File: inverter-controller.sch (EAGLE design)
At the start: 187 parts, among them IC1 STM32F334C8T6, IC2 SY7152ABC, IC3 LMV358MMX, IC4 LMV358MMX, IC5 SY7152ABC, J1 621006245821, J2 61300211121, K1 FINDER_34.51.7.024.0010FINDER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, K2 FINDER_34.51.7.024.0010FINDER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, K3 FINDER_34.51.7.024.0010FINDER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, U1 DIODES_AP3015KTR-G1DIODES_AP3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, X1 0289-9066**15EDGVC-3.81-02P-14, X2 0289-9066**15EDGVC-3.81-02P-14, X3 0289-9066**15EDGVC-3.81-02P-14, X4 0289-9066**15EDGVC-3.81-02P-14, X5 1365-10, X6 1365-16, X7 1365-10, X8 1365-10, Y1 NX2016SA-32M

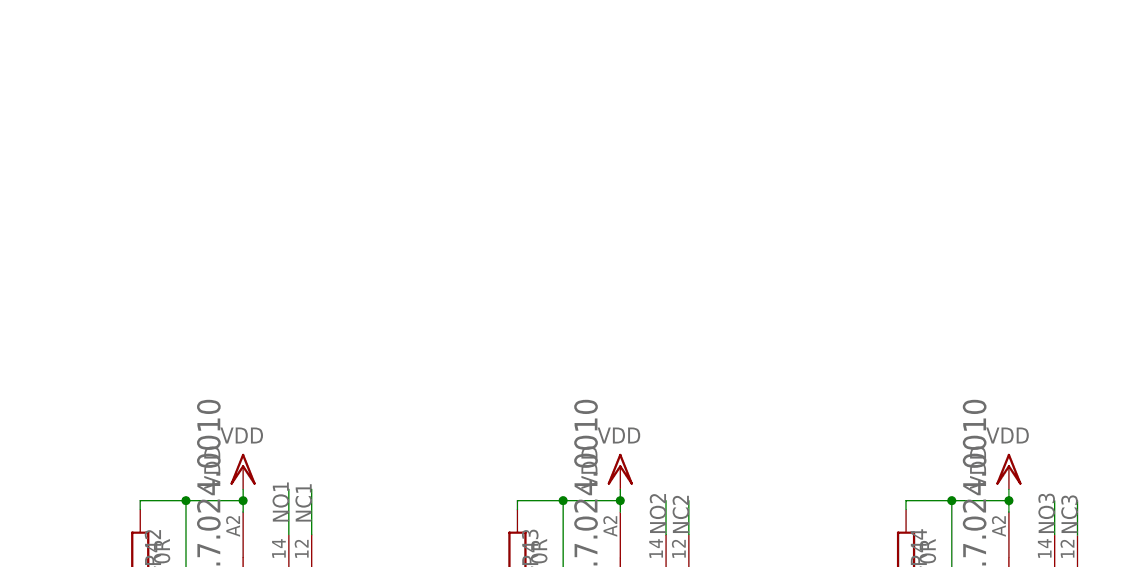
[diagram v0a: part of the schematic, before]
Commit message: Relay soketleri eklendi.
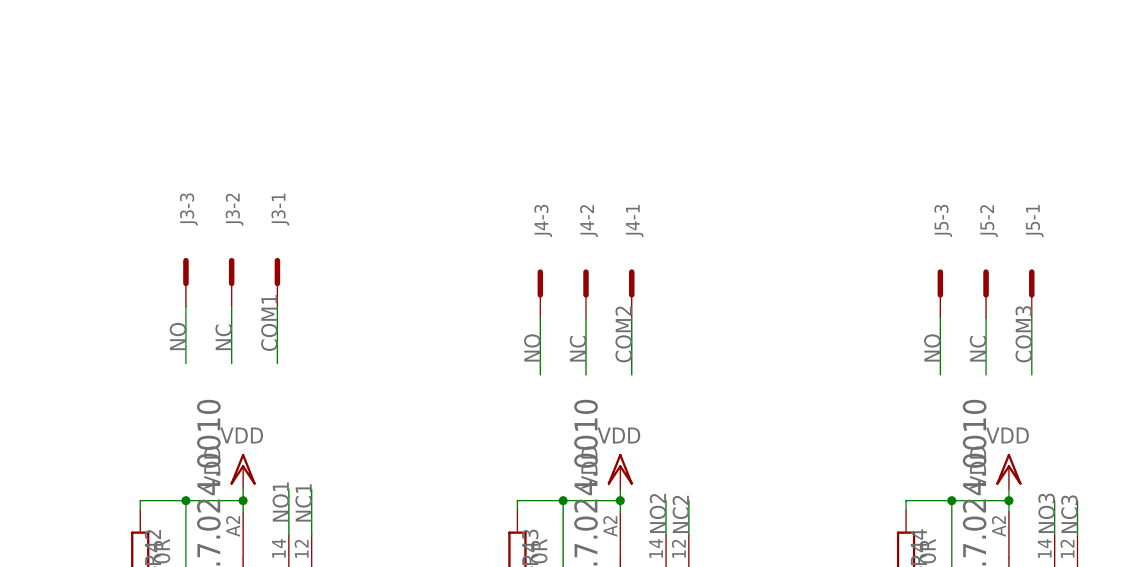
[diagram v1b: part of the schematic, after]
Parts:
- added J3, J4, J5: MCV3, con-phoenix-381:MCV3
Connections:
- new net NC: J3-2.SK, J4-2.SK, J5-2.SK
- new net NO: J3-3.SK, J4-3.SK, J5-3.SK
- net COM1: now also J3-1.SK
- net COM2: now also J4-1.SK
- net COM3: now also J5-1.SK
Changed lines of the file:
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@@
 <part name="GND48" library="supply1" library_urn="urn:adsk.eagle:library:371" deviceset="GND" device=""/>
 <part name="GND49" library="supply1" library_urn="urn:adsk.eagle:library:371" deviceset="GND" device=""/>
+<part name="J3" library="con-phoenix-381" library_urn="urn:adsk.eagle:library:27486877" deviceset="MCV3" device="" package3d_urn="urn:adsk.eagle:package:27487037/1"/>
+<part name="J4" library="con-phoenix-381" library_urn="urn:adsk.eagle:library:27486877" deviceset="MCV3" device="" package3d_urn="urn:adsk.eagle:package:27487037/1"/>
+<part name="J5" library="con-phoenix-381" library_urn="urn:adsk.eagle:library:27486877" deviceset="MCV3" device="" package3d_urn="urn:adsk.eagle:package:27487037/1"/>
 </parts>
 <sheets>
@@
 <attribute name="VALUE" x="179.07" y="145.288" size="1.778" layer="96" rot="R270"/>
 </instance>
+<instance part="J3" gate="-1" x="387.35" y="261.62" smashed="yes" rot="R270">
+<attribute name="NAME" x="386.715" y="271.78" size="1.524" layer="95" rot="R270"/>
+</instance>
+<instance part="J3" gate="-2" x="382.27" y="261.62" smashed="yes" rot="R270">
+<attribute name="NAME" x="381.635" y="271.78" size="1.524" layer="95" rot="R270"/>
+</instance>
+<instance part="J3" gate="-3" x="377.19" y="261.62" smashed="yes" rot="R270">
+<attribute name="NAME" x="376.555" y="271.78" size="1.524" layer="95" rot="R270"/>
+</instance>
+<instance part="J4" gate="-1" x="426.72" y="260.35" smashed="yes" rot="R270">
+<attribute name="NAME" x="426.085" y="270.51" size="1.524" layer="95" rot="R270"/>
+</instance>
+<instance part="J4" gate="-2" x="421.64" y="260.35" smashed="yes" rot="R270">
+<attribute name="NAME" x="421.005" y="270.51" size="1.524" layer="95" rot="R270"/>
+</instance>
+<instance part="J4" gate="-3" x="416.56" y="260.35" smashed="yes" rot="R270">
+<attribute name="NAME" x="415.925" y="270.51" size="1.524" layer="95" rot="R270"/>
+</instance>
+<instance part="J5" gate="-1" x="471.17" y="260.35" smashed="yes" rot="R270">
+<attribute name="NAME" x="470.535" y="270.51" size="1.524" layer="95" rot="R270"/>
+</instance>
+<instance part="J5" gate="-2" x="466.09" y="260.35" smashed="yes" rot="R270">
+<attribute name="NAME" x="465.455" y="270.51" size="1.524" layer="95" rot="R270"/>
+</instance>
+<instance part="J5" gate="-3" x="461.01" y="260.35" smashed="yes" rot="R270">
+<attribute name="NAME" x="460.375" y="270.51" size="1.524" layer="95" rot="R270"/>
+</instance>
 </instances>
 <busses>
@@
 <label x="388.62" y="212.09" size="1.778" layer="95" rot="R90"/>
 </segment>
+<segment>
+<pinref part="J3" gate="-1" pin="SK"/>
+<wire x1="387.35" y1="259.08" x2="387.35" y2="252.73" width="0.1524" layer="91"/>
+<label x="387.35" y="254" size="1.778" layer="95" rot="R90"/>
+</segment>
 </net>
 <net name="NO2" class="0">
@@
 <label x="430.53" y="212.09" size="1.778" layer="95" rot="R90"/>
 </segment>
+<segment>
+<pinref part="J4" gate="-1" pin="SK"/>
+<wire x1="426.72" y1="257.81" x2="426.72" y2="251.46" width="0.1524" layer="91"/>
+<label x="426.72" y="252.73" size="1.778" layer="95" rot="R90"/>
+</segment>
 </net>
 <net name="COM3" class="0">
@@
 <label x="473.71" y="212.09" size="1.778" layer="95" rot="R90"/>
 </segment>
+<segment>
+<pinref part="J5" gate="-1" pin="SK"/>
+<wire x1="471.17" y1="257.81" x2="471.17" y2="251.46" width="0.1524" layer="91"/>
+<label x="471.17" y="252.73" size="1.778" layer="95" rot="R90"/>
+</segment>
 </net>
 <net name="NO3" class="0">
@@
 </segment>
 </net>
+<net name="NC" class="0">
+<segment>
+<pinref part="J3" gate="-2" pin="SK"/>
+<wire x1="382.27" y1="259.08" x2="382.27" y2="252.73" width="0.1524" layer="91"/>
+<label x="382.27" y="254" size="1.778" layer="95" rot="R90"/>
+</segment>
+<segment>
+<pinref part="J4" gate="-2" pin="SK"/>
+<wire x1="421.64" y1="257.81" x2="421.64" y2="251.46" width="0.1524" layer="91"/>
+<label x="421.64" y="252.73" size="1.778" layer="95" rot="R90"/>
+</segment>
+<segment>
+<pinref part="J5" gate="-2" pin="SK"/>
+<wire x1="466.09" y1="257.81" x2="466.09" y2="251.46" width="0.1524" layer="91"/>
+<label x="466.09" y="252.73" size="1.778" layer="95" rot="R90"/>
+</segment>
+</net>
+<net name="NO" class="0">
+<segment>
+<pinref part="J3" gate="-3" pin="SK"/>
+<wire x1="377.19" y1="259.08" x2="377.19" y2="252.73" width="0.1524" layer="91"/>
+<label x="377.19" y="254" size="1.778" layer="95" rot="R90"/>
+</segment>
+<segment>
+<pinref part="J4" gate="-3" pin="SK"/>
+<wire x1="416.56" y1="257.81" x2="416.56" y2="251.46" width="0.1524" layer="91"/>
+<label x="416.56" y="252.73" size="1.778" layer="95" rot="R90"/>
+</segment>
+<segment>
+<pinref part="J5" gate="-3" pin="SK"/>
+<wire x1="461.01" y1="257.81" x2="461.01" y2="251.46" width="0.1524" layer="91"/>
+<label x="461.01" y="252.73" size="1.778" layer="95" rot="R90"/>
+</segment>
+</net>

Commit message: Mekanik kistaslar belirlendi.
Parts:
- removed D7: (no value), diode:DIODE-SOD80C
- removed J5: MCV3, con-phoenix-381:MCV3
- removed K3: FINDER_34.51.7.024.0010FINDER_34.51.7.024.0010_0_0, Finder - 34.51.7.024.0010:FINDER_34.51.7.024.0010FINDER_34.51.7.024.0010_0_0
- removed LED3: (no value), adafruit:LEDCHIPLED_0805
- removed Q3: (no value), adafruit:MOSFET-NREFLOW
- removed R40: (no value), rcl:R-EU_R0603
- removed R41: 22R, rcl:R-EU_R0603
- removed R44: 470R, rcl:R-EU_R0603
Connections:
- removed net COM3: J5-1.SK, K3.11
- removed net N$28: Q3.G, R40.2, R41.1
- removed net N$31: D7.A, K3.A1, LED3.C, Q3.D
- removed net N$33: LED3.A, R44.1
- removed net NC3: K3.12
- removed net NO3: K3.14
- net GND: no longer Q3.S, R40.1
- net NC: no longer J5-2.SK
- net NO: no longer J5-3.SK
- net RELAY3: no longer R41.2
- net VDD: no longer D7.C, K3.A2, R44.2

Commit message: Mini kart tasarimi icin sadelestirildi.
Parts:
- removed C20, C60, C63: 100n, rcl:C-EUC0603
- removed C59: 1019-3366**CAP 0603 CER 10uF 16V %20 X5R, rcl:C-EUC0603
- removed C61: 10n, rcl:C-EUC0603
- removed C62: 1n, rcl:C-EUC0603
- removed C64: 1u, rcl:C-EUC1206
- removed D5, D6: (no value), diode:DIODE-SOD80C
- removed D9: 1119-3055, Diode:DIODEDO-214AC(SMA)
- removed J3, J4: MCV3, con-phoenix-381:MCV3
- removed K1, K2: FINDER_34.51.7.024.0010FINDER_34.51.7.024.0010_0_0, Finder - 34.51.7.024.0010:FINDER_34.51.7.024.0010FINDER_34.51.7.024.0010_0_0
- removed L2: 1319-4102**INDUCTOR POWER 22UH 4X4X1.8MM SMD, wuerth-elektronik:WE-PD2_S
- removed LED1, LED11, LED2, LED4, LED5, LED6: (no value), adafruit:LEDCHIPLED_0805
- removed Q1, Q2: (no value), adafruit:MOSFET-NREFLOW
- removed R16, R37, R38: (no value), rcl:R-EU_R0603
- removed R36, R39: 22R, rcl:R-EU_R0603
- removed R42, R43: 470R, rcl:R-EU_R0603
- removed R45, R46, R47: 100R, rcl:R-EU_R0603
- removed R67: 2M, rcl:R-EU_R0603
- removed R68: 130K, rcl:R-EU_R0603
- removed R69: 1k, rcl:R-EU_R0603
- removed R73: NC, rcl:R-EU_R0603
- removed U1: DIODES_AP3015KTR-G1DIODES_AP3015KTR-G1_0_0, AP3015KTR-G1:DIODES_AP3015KTR-G1DIODES_AP3015KTR-G1_0_0
- removed X3: 0289-9066**15EDGVC-3.81-02P-14, con-phoenix-381_l:MCV2
- removed X5, X7, X8: 1365-10, con-leotronics:1365-10
- R56: value (none) -> 220R
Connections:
- removed net CAN_RX: IC1.PB8, X5-7.S, X5-8.S
- removed net CAN_TX: IC1.PB9, X5-5.S, X5-6.S
- removed net COM1: J3-1.SK, K1.11
- removed net COM2: J4-1.SK, K2.11
- removed net N$22: LED2.A, R43.1
- removed net N$24: Q1.G, R36.1, R37.2
- removed net N$25: Q2.G, R38.2, R39.1
- removed net N$26: LED5.A, R46.1
- removed net N$27: LED1.A, R42.1
- removed net N$29: D5.A, K1.A1, LED1.C, Q1.D
- removed net N$30: D6.A, K2.A1, LED2.C, Q2.D
- removed net N$32: LED6.A, R47.1
- removed net N$37: LED4.A, R45.1
- removed net N$44: D9.A, L2.1, U1.SW
- removed net N$45: R67.1, R68.2, U1.FB
- removed net N$49: LED11.A, R69.1
- removed net N$50: C59.1, C60.1, C61.1, L2.2, R73.2, U1.VIN
- removed net NC: J3-2.SK, J4-2.SK
- removed net NC1: K1.12
- removed net NC2: K2.12
- removed net NO: J3-3.SK, J4-3.SK
- removed net NO1: K1.14
- removed net NO2: K2.14
- removed net RELAY1: IC1.PB10, R36.2
- removed net RELAY2: IC1.PB11, R39.2
- removed net SPI1_CS: IC1.PA15, X8-10.S, X8-9.S
- removed net SPI1_MISO: IC1.PB4, X8-5.S, X8-6.S
- removed net SPI1_MOSI: IC1.PB5, X8-3.S, X8-4.S
- removed net USART1_RX: IC1.PB7, X7-7.S, X7-8.S
- removed net USART1_TX: IC1.PB6, X7-5.S, X7-6.S
- removed net VDD: C62.1, C63.1, C64.1, D5.C, D6.C, D9.C, K1.A2, K2.A2, R42.2, R43.2, R67.2, R69.2
- net +3V3: now also X6-1.S; no longer R73.1, X3.1.SK, X5-1.S, X5-2.S, X6-2.S, X7-1.S, X7-2.S, X8-1.S
- net DGND: now also X6-2.S; no longer X5-10.S, X5-3.S, X5-4.S, X5-9.S, X6-1.S, X7-3.S, X7-4.S, X8-2.S
- net DRV1_EN: now also X6-10.S; no longer X6-9.S
- net DRV2_EN: now also X6-4.S; no longer X6-3.S
- net G11_PWM: now also X6-14.S; no longer X6-13.S
- net G12_PWM: now also X6-12.S; no longer X6-11.S
- net G13_PWM: now also X6-8.S; no longer X6-7.S
- net G14_PWM: now also X6-6.S; no longer X6-5.S
- net GND: no longer C20.2, C59.2, C60.2, C61.2, C62.2, C63.2, C64.2, LED11.C, LED4.C, LED5.C, LED6.C, Q1.S, Q2.S, R37.1, R38.1, R68.1, R8.1, U1.GND
- net IA_SENS: now also X6-7.S; no longer X6-8.S
- net IB_SENS: now also X6-3.S; no longer X6-4.S
- net IIN_SENS: now also R8.1, X6-16.S; no longer R16.2, X6-15.S
- net I_IN: now also R8.2; no longer R16.1
- net N$13: no longer R45.2
- net N$14: no longer R46.2
- net N$20: no longer R47.2
- net NTC2: no longer C20.1, R8.2, X3.2.SK
- net RELAY_EN: no longer IC1.PA14, U1.!SHDN!
- net SPI1_SCK: no longer IC1.PB3, X8-7.S, X8-8.S
- net USART1_DIR: no longer X7-10.S, X7-9.S
- net VA_SENS: now also X6-9.S; no longer X6-10.S
- net VB_SENS: now also X6-5.S; no longer X6-6.S
- net VIN_2: now also R15.2; no longer R15.1
- net VIN_SENS: now also R15.1, X6-15.S; no longer R15.2, X6-16.S
- net VIN_SENS_DIFF: now also X6-13.S; no longer X6-14.S
- net VOUT_SENS_DIFF: now also X6-11.S; no longer X6-12.S
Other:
- note removed: "Haberlesme Kart Baglantilari"
- note removed: "Relay Coil Supply"
- note removed: "Relays"
- moved on the sheet: C33, C34, C35, C36, R15, R8, X6-1, X6-10, X6-11, X6-12, X6-13, X6-14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

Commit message: Direnc ve kondansator kutuphaneleri degistirildi(silk sorunu nedeniyle).
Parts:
- removed C58: 100n, rcl:C-EUC0603
- removed LED10, LED7, LED9: (no value), adafruit:LEDCHIPLED_0805
- removed R51, R52, R62, R63, R64: 33R, rcl:R-EU_R0603
- removed R53, R54, R65, R66: 1k, rcl:R-EU_R0603
- removed R55, R76: 470R, rcl:R-EU_R0603
- removed R56: 220R, rcl:R-EU_R0603
- removed R57: 1M, rcl:R-EU_R0603
- removed R58: 200k, rcl:R-EU_R0603
- removed R59: 10.5k, rcl:R-EU_R0603
- removed R60, R61: 0R, rcl:R-EU_R0603
- removed R71, R75: NC, rcl:R-EU_R0603
- added C20: 10nF, rcl:C-EUC0603E
- added LED1, LED2, LED3: (no value), adafruit:LEDCHIP-LED0805
- added R16: 220R, rcl:R-EU_R0603E
- added R36, R37: 470R, rcl:R-EU_R0603E
- added R38, R39, R47: 33R, rcl:R-EU_R0603E
- added R40, R44: 1K, rcl:R-EU_R0603E
- added R41: 1M, rcl:R-EU_R0603E
- added R42: 200K, rcl:R-EU_R0603E
- added R43: 10.5K, rcl:R-EU_R0603E
- added R45, R46: 0R, rcl:R-EU_R0603E
- C1, C2: value (none) -> 10pF; device rcl:C-EUC0603 -> rcl:C-EUC0603E
- C10, C13, C19, C37, C38, C47: value 100n -> 100nF; device rcl:C-EUC0603 -> rcl:C-EUC0603E
- C11: value 4.7u -> 4.7uF; device rcl:C-EUC0603 -> rcl:C-EUC0603E
- C12: value 1019-3366**CAP 0603 CER 10uF 16V %20 X5R -> 10uF; device rcl:C-EUC0603 -> rcl:C-EUC0603E
- C14, C3, C39, C48, C5, C52, C57: value 10n -> 10nF; device rcl:C-EUC0603 -> rcl:C-EUC0603E
- C15, C16, C54: value 10u -> 10uF; device rcl:C-EUC0805 -> rcl:C-EUC0603E
- C17, C22, C24, C26, C28, C30, C32, C34, C42, C45, C51: value 100n -> 10nF; device rcl:C-EUC0603 -> rcl:C-EUC0603E
- C18, C21, C23, C25, C27, C29, C31, C33, C35, C43, C46, C56: value 10n -> 100nF; device rcl:C-EUC0603 -> rcl:C-EUC0603E
- C36: value 100n -> 120pF; device rcl:C-EUC0603 -> rcl:C-EUC0603E
- C4: value 1u -> 1uF; device rcl:C-EUC0603 -> rcl:C-EUC0603E
- C40: value 120p -> 100nF; device rcl:C-EUC0603 -> rcl:C-EUC0603E
- C41, C44: value 120p -> 120pF; device rcl:C-EUC0603 -> rcl:C-EUC0603E
- C49, C55: value 100n -> 10uF; device rcl:C-EUC0603 -> rcl:C-EUC0603E
- C50: value 1019-3366**CAP 0603 CER 10uF 16V %20 X5R -> 100nF; device rcl:C-EUC0603 -> rcl:C-EUC0603E
- C53: value 10u -> 100nF; device rcl:C-EUC0805 -> rcl:C-EUC0603E
- C6, C8: value 100n -> 4.7uF; device rcl:C-EUC0603 -> rcl:C-EUC0603E
- C7, C9: value 4.7u -> 100nF; device rcl:C-EUC0603 -> rcl:C-EUC0603E
- R1, R32: value (none) -> 1K; device rcl:R-EU_R0603 -> rcl:R-EU_R0603E
- R10, R11, R12, R13, R14, R15, R17, R18, R19, R2, R20, R21, R22, R23, R24, R25, R26, R27, R28, R29, R30, R31, R4, R7, R8, R9: device rcl:R-EU_R0603 -> rcl:R-EU_R0603E
- R3: value 10k -> 10K; device rcl:R-EU_R0603 -> rcl:R-EU_R0603E
- R33, R34: value (none) -> 0R; device rcl:R-EU_R0603 -> rcl:R-EU_R0603E
- R35: value (none) -> 33R; device rcl:R-EU_R0603 -> rcl:R-EU_R0603E
- R48, R49: value 0R -> 33R; device rcl:R-EU_R0603 -> rcl:R-EU_R0603E
- R5: value 200k -> 200K; device rcl:R-EU_R0603 -> rcl:R-EU_R0603E
- R50: value 33R -> 1K; device rcl:R-EU_R0603 -> rcl:R-EU_R0603E
- R6: value 10.5k -> 10.5K; device rcl:R-EU_R0603 -> rcl:R-EU_R0603E
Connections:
- removed net HRTIM1_CHA1: IC1.PA8, R17.1
- removed net HRTIM1_CHA2: IC1.PA9, R18.1
- removed net HRTIM1_CHB1: IC1.PA10, R19.1
- removed net HRTIM1_CHB2: IC1.PA11, R20.1
- removed net N$39: LED9.A, R56.2
- removed net N$48: C12.1, C13.1, C14.1, IC2.IN, L4.2, R71.2
- removed net N$51: C50.1, C51.1, C52.1, IC5.IN, L1.2, R75.2
- new net N$22: LED1.A, R16.2
- net +12V/1: now also R32.1, R33.2, R34.2, R5.1; no longer R48.2, R49.2, R5.2, R54.1
- net +12V/2: now also C52.1, R42.1, R44.1, R45.2, R46.2; no longer C56.1, R58.2, R60.2, R61.2, R66.1
- net +3V3: now also C12.1, C13.1, C14.1, C46.1, C49.1, C50.1, C51.1, C6.1, C7.1, IC2.IN, IC5.IN, L1.2, L4.2, R16.1, R18.1, R36.1, R37.1; no longer C47.1, C6.2, C7.2, R33.1, R55.1, R56.1, R71.1, R75.1, R76.1
- net FAN2_EN: now also R41.2; no longer R57.2
- net G11_PWM: now also IC1.PA8; no longer R17.2
- net G12_PWM: now also IC1.PA9; no longer R18.2
- net G13_PWM: now also IC1.PA10; no longer R19.2
- net G14_PWM: now also IC1.PA11; no longer R20.2
- net GND: now also C19.1, C20.2, C40.2, C6.2, C7.2, LED1.C, LED2.C, LED3.C, R19.2, R24.2, R29.2, R35.2, R38.2, R39.2, R41.1, R43.2, R47.2, R48.2, R49.2, R6.2, R7.2; no longer C19.2, C36.2, C58.2, C6.1, C7.1, LED10.C, LED7.C, LED9.C, R24.1, R29.1, R34.1, R50.2, R51.2, R52.2, R57.1, R59.1, R6.1, R62.2, R63.2, R64.2, R7.1
- net IA: now also C26.1, R17.1; no longer C28.1, R21.1
- net IB: now also C30.1, R22.1; no longer C32.1, R27.1
- net IIN_SENS: now also R8.2; no longer R8.1
- net I_FAN: now also C47.1, C56.1, R40.2, R50.2; no longer C49.1, C58.1, R53.2, R65.2
- net I_IN: now also C34.1, R27.1, R8.1; no longer C36.1, R32.1, R8.2
- net N$1: now also C36.2, R20.1, R21.2; no longer C40.2, R22.2, R25.1
- net N$10: now also R35.1, R38.1, R39.1, R40.1; no longer R50.1, R51.1, R52.1, R53.1
- net N$13: now also R20.2; no longer R25.2
- net N$14: now also C42.1, R26.2; no longer C43.1, R30.2
- net N$15: now also R18.2, R19.1; no longer R23.2, R24.2
- net N$16: now also R22.2, R25.1; no longer R26.1, R27.2
- net N$17: now also R27.2, R30.1; no longer R31.1, R32.2
- net N$18: now also C40.1, R23.2, R24.1; no longer C42.1, R28.2, R29.2
- net N$19: now also R25.2, R26.1; no longer R26.2, R30.1
- net N$20: now also C45.1, R31.2; no longer C46.1, R35.2
- net N$21: now also C43.1, R28.2, R29.1; no longer C45.1, R33.2, R34.2
- net N$23: now also R30.2, R31.1; no longer R31.2, R35.1
- net N$34: now also R33.1, R34.1; no longer R48.1, R49.1
- net N$35: now also R36.2; no longer R76.2
- net N$40: now also R42.2, R43.1; no longer R58.1, R59.2
- net N$41: now also R45.1, R46.1; no longer R60.1, R61.1
- net N$42: now also R47.1, R48.1, R49.1, R50.1; no longer R62.1, R63.1, R64.1, R65.1
- net N$43: now also LED3.A, R44.2; no longer LED10.A, R66.2
- net N$47: now also R37.2; no longer R55.2
- net N$7: now also C36.1, R17.2, R21.1; no longer C40.1, R21.2, R22.1
- net N$8: now also R5.2, R6.1; no longer R5.1, R6.2
- net N$9: now also LED2.A, R32.2; no longer LED7.A, R54.2
- net NTC1: now also C19.2, R7.1; no longer C19.1, R7.2
- net VA: now also C24.1; no longer C26.1
- net VB: now also C28.1; no longer C30.1
- net VIN_1: now also C20.1; no longer C22.1
- net VIN_2: now also C32.1; no longer C34.1
- net VOUT: now also C22.1; no longer C24.1
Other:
- note added: "CHA1"
- note added: "CHA2"
- note added: "CHB1"
- note added: "CHB2"
- moved on the sheet: C17, C18, C19, C21, C22, C23, C24, C25, C26, C27, C28, C29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
